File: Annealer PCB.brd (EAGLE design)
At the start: 53.3 x 77.5 mm, 36 parts

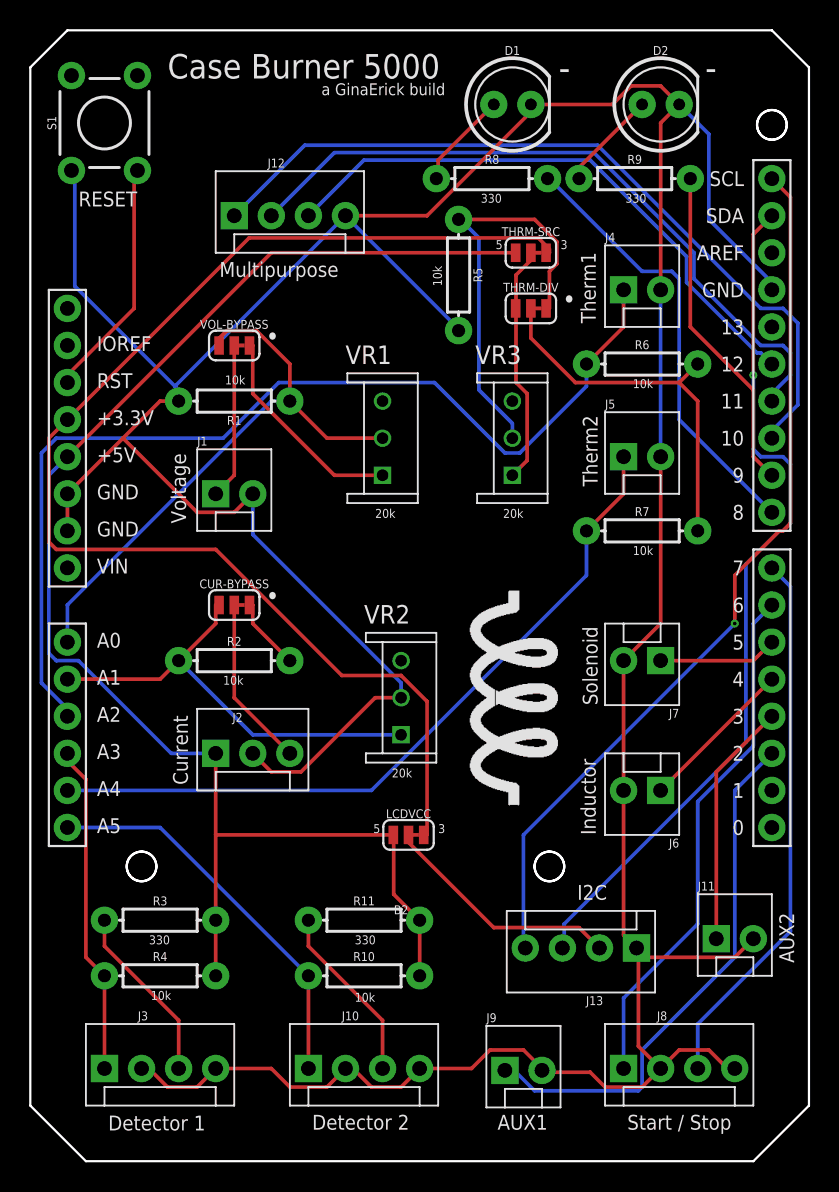
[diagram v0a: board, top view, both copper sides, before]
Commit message: v3.1 - source voltage for phototransistors
Source voltage was only 5v on v3.0. Changed design so that source voltage for thermistors AND phototransistors on the proximity sensors is fed by an appropriate reference voltage.
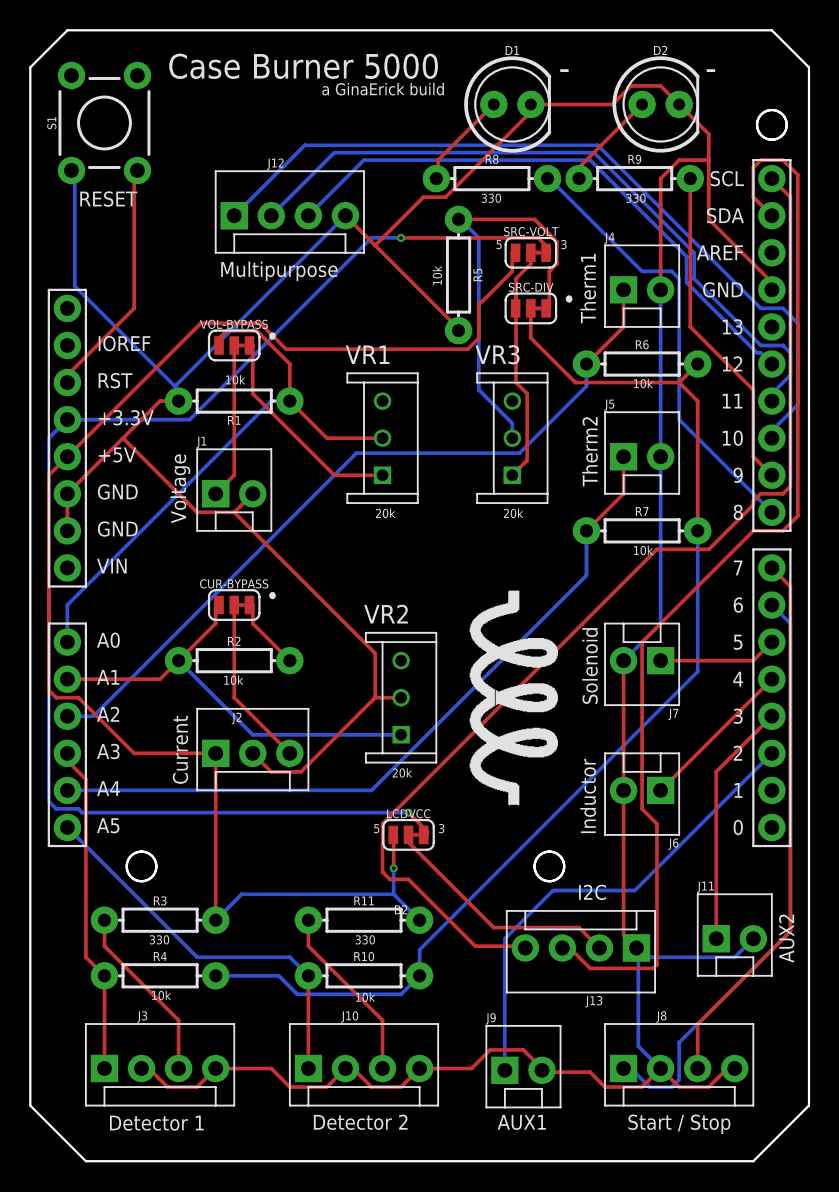
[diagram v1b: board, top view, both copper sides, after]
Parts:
- renumbered THRM-DIV to SRC-DIV, THRM-SRC to SRC-VOLT
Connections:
- removed net N$1: R6.P$2, R7.P$2, SRC-DIV.2
- new net SRC: R10.P$2, R4.P$2, R6.P$2, R7.P$2, SRC-DIV.2
- net 5V: no longer R10.P$2, R4.P$2
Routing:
- net SRC: track 0.00 -> 79.3 mm
- net N$1: track 25.9 -> 0.00 mm
- net A2: track 69.7 -> 52.6 mm
- net SDA: track 59.3 -> 74.8 mm, vias 1 -> 0
- net SCL: track 61.0 -> 74.5 mm, vias 1 -> 0
- net 3.3V: track 87.7 -> 92.9 mm, vias 0 -> 2
- net D6: track 36.0 -> 40.7 mm
- net GND: track 269.7 -> 265.3 mm
- net D2: track 36.7 -> 32.6 mm
- net 5V: track 102.6 -> 100.8 mm, vias 0 -> 1
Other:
- board text added: "Version 3.1"
- board text removed: "Version 3.0"

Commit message: v3.2 - source voltage for proximity detectors
Changed voltage handling for proximity sensors to avoid disrupting thermistor measurements when a phototransistor detects light inbound. Each phototransistor should have it's own input source and voltage divider. The thermistors share a common, separate input. Voltage dividers on each are bypassable.
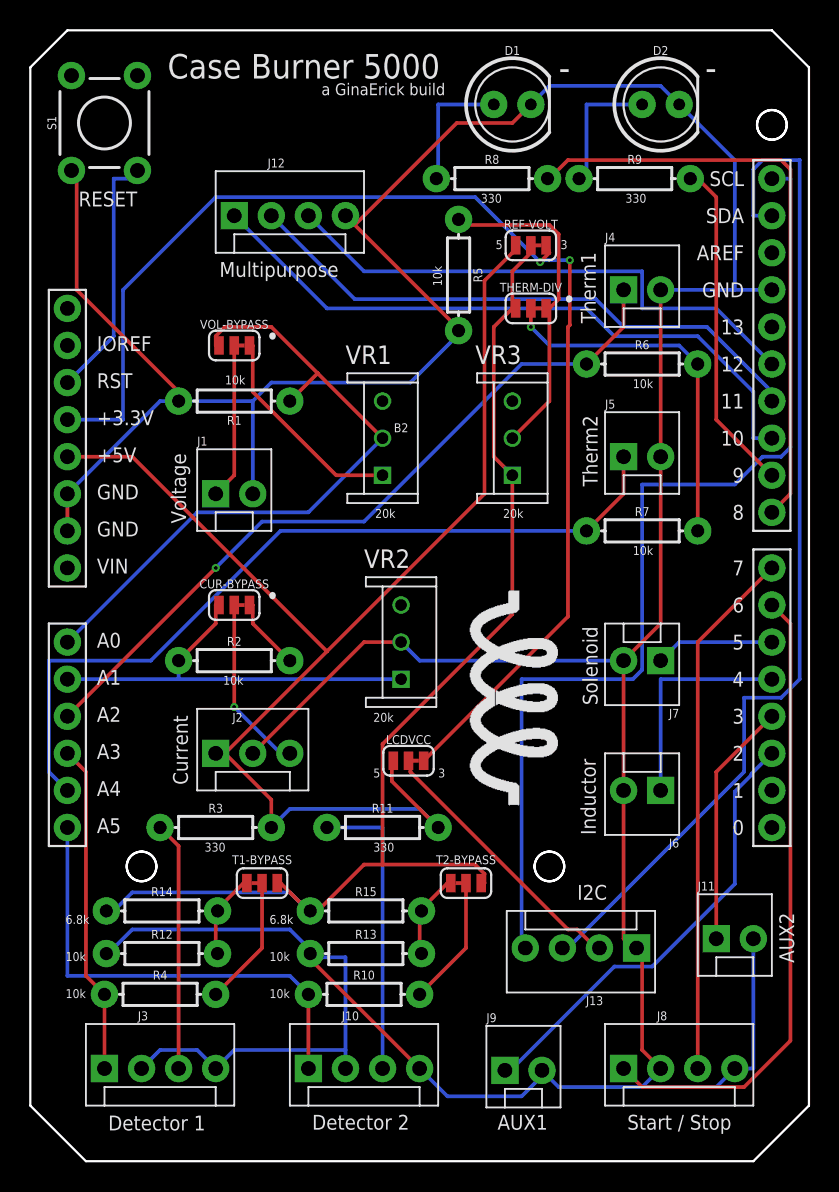
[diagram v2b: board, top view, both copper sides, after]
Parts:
- removed SRC-VOLT: JUMPER-SMT_3_1-NC_TRACE_SILK, SparkFun-Jumpers:SMT-JUMPER_3_1-NC_TRACE_SILK
- added R12, R13: 10k, SparkFun-Resistors:AXIAL-0.3
- added R14, R15: 6800, SparkFun-Resistors:AXIAL-0.3
- added REF-VOLT, T1-BYPASS, T2-BYPASS: JUMPER-SMT_3_1-NC_TRACE_SILK, SparkFun-Jumpers:SMT-JUMPER_3_1-NC_TRACE_SILK
- moved R3 7.41 mm to (21.6, 25.4)
- moved R11 6.48 mm to (33.0, 25.4)
- moved LCDVCC 5.08 mm to (34.8, 30.0)
- moved VR2 3.81 mm to (34.3, 38.1)
- moved R10 1.27 mm to (31.8, 14.0)
- moved R4 1.27 mm to (17.8, 14.0)
- renumbered SRC-DIV to THERM-DIV
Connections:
- new net N$1: R4.P$2, T1-BYPASS.2
- new net N$11: R12.P$2, R14.P$2, T1-BYPASS.3
- new net N$13: R13.P$2, R15.P$2, T2-BYPASS.3
- new net VREF: R14.P$1, R15.P$1, REF-VOLT.2, T1-BYPASS.1, T2-BYPASS.1, THERM-DIV.1, VR3.1
- net 3.3V: now also REF-VOLT.3; no longer SRC-VOLT.3
- net 5V: now also REF-VOLT.1; no longer SRC-VOLT.1
- net GND: now also R12.P$1, R13.P$1
- net N$8: now also R10.P$2, T2-BYPASS.2; no longer SRC-VOLT.2, THERM-DIV.1, VR3.1
- net SRC: no longer R10.P$2, R4.P$2
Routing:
- net VREF: track 0.00 -> 80.4 mm
- net SRC: track 79.3 -> 25.2 mm, vias 0 -> 1
- net GND: track 265.3 -> 292.2 mm
- net D8: track 30.5 -> 41.4 mm
- net D10: track 54.3 -> 45.0 mm
- net 5V: track 100.8 -> 91.7 mm, vias 1 -> 0
- net N$1: track 0.00 -> 8.94 mm
- net N$6: track 12.3 -> 20.3 mm
- net D11: track 47.9 -> 39.9 mm
- net N$8: track 16.4 -> 8.94 mm
- net N$10: track 29.0 -> 22.8 mm
- net N$11: track 0.00 -> 5.99 mm
- net N$13: track 0.00 -> 5.99 mm
- net A0: track 40.0 -> 45.8 mm
- net A4: track 50.8 -> 56.1 mm
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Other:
- board text added: "6.8k"
- board text added: "Version 3.2"
- board text removed: "Version 3.1"
